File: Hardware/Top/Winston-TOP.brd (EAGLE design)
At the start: 38 x 38 mm, 52 parts, among them SW1 SWITCH.MOM, SW2 SWITCH.MOM, SW5 SWITCH.MOM, U2 NRF52832_MODULE_MDBT42, U4 PCF8523

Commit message: updated Hardware files
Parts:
- added C22: 100n, LinnesLab-Passives:C0603
- added C23, C24: 47p, LinnesLab-Passives:C0603
- added JP2: (no value), LinnesLab-Switches:SMT-JUMPER_2_NO_SILK
- added LED5: RED, LinnesLab-LED:LED-0603
- added LED6: YELLOW, LinnesLab-LED:LED-0603
- added R1, R2: 0, LinnesLab-Passives:R0603
- added R17, R18: 27, LinnesLab-Passives:R0603
- added R19, R20: 1k, LinnesLab-Passives:R0603
- added U5: FT231XS, LinnesLab-DigitalIC:SSOP20_L
- R8, R9: value 10k -> 10K
- moved R9 57.9 mm to (-16.1, -19.4), turned to 0 degrees
- moved R8 55.5 mm to (-16.1, -16.7), turned to 0 degrees
- moved L2 2.19 mm to (20.3, 25.8)
- moved U2 1.08 mm to (31.5, 29.2)
- moved C16 0.66 mm to (23.0, 26.0)
- moved C7 0.53 mm to (24.5, 26.0)
- moved R3 0.49 mm to (40.0, 24.9)
- moved C18 0.32 mm to (21.8, 25.6)
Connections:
- removed net RXD: U2.21
- removed net TXD: U2.19
- new net !CTS: JP2.2, U5.9
- new net FT3V3: U5.13
- new net N$23: R17.2, U5.12
- new net N$24: R18.2, U5.11
- new net N$25: LED5.C, R19.2
- new net N$26: LED6.C, R20.2
- new net RXD.FT: R2.1, U5.4
- new net RXD.NRF: R1.2, U2.21
- new net RXLED: R19.1, U5.17
- new net TXD.FT: R1.1, U5.20
- new net TXD.NRF: R2.2, U2.19
- new net TXLED: R20.1, U5.10
- net 3.3V: now also C22.2, LED5.A, LED6.A, U5.14, U5.3
- net DTR: now also U5.1
- net GND: now also C22.1, C23.2, C24.1, JP2.1, U5.16, U5.6
- net SCL: now also R9.1; no longer R8.1
- net SDA: now also R8.1; no longer R9.1
- net USB+: now also C23.1, R18.1
- net USB-: now also C24.2, R17.1
- net V_USB: now also U5.15

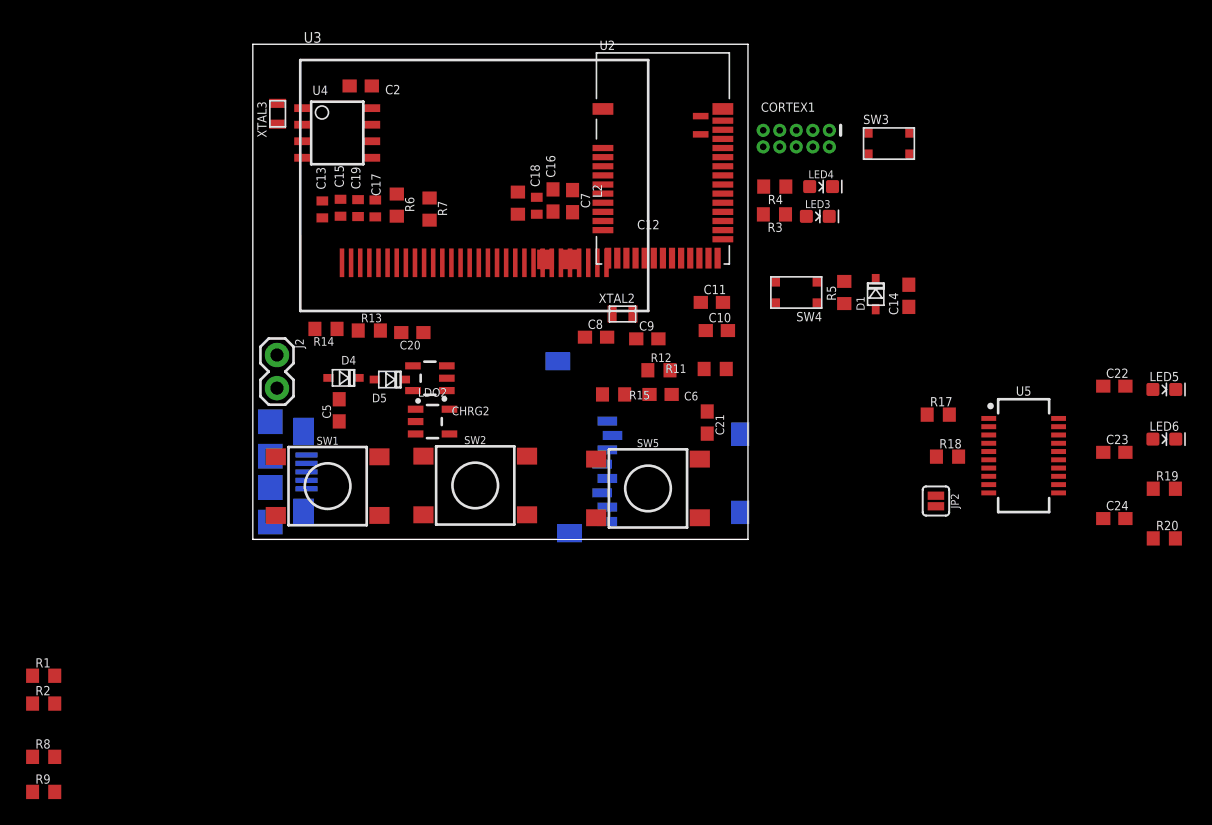
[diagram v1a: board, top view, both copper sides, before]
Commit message: updated top and bottom boards with everything from Take 002
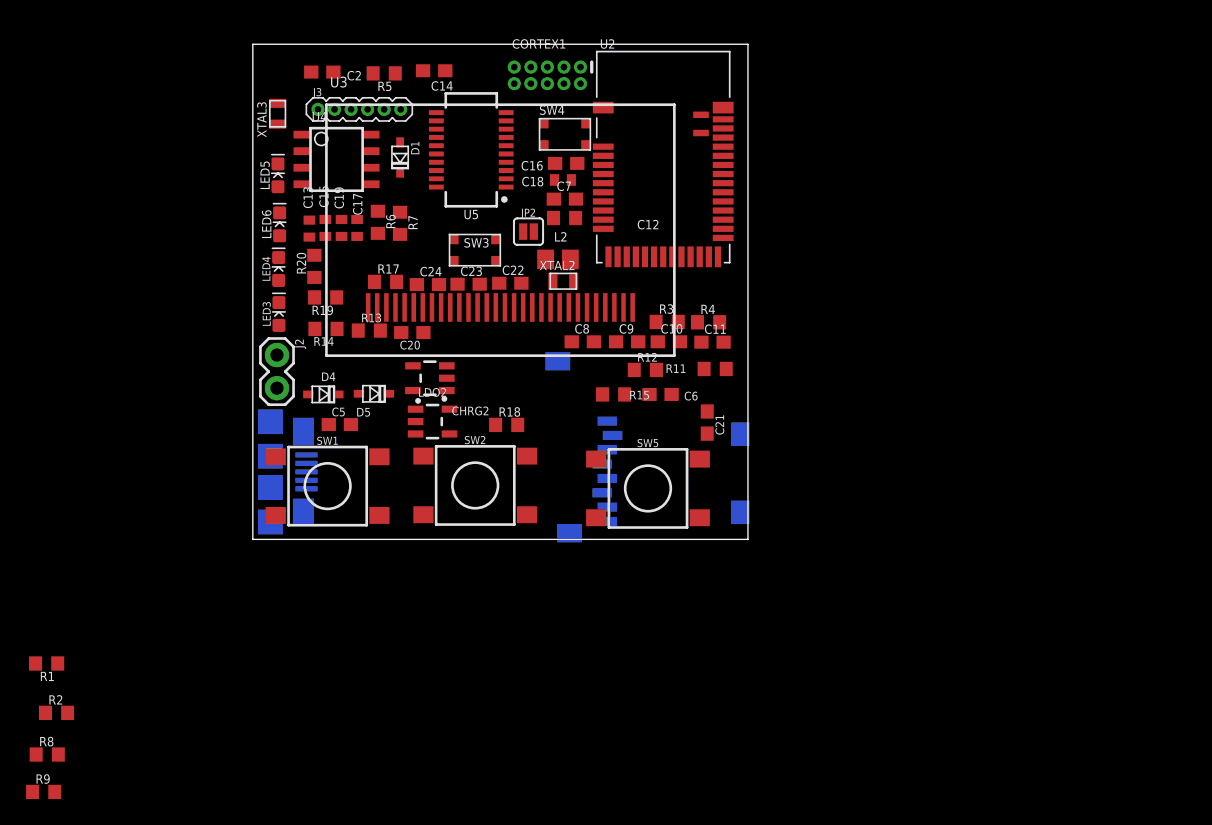
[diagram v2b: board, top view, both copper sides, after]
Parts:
- added J3: (no value), LinnesLab-Connectors:1X06_1.27MM
- moved LED5 70.0 mm to (1.93, 27.9), turned to 90 degrees
- moved LED6 69.9 mm to (2.06, 24.2), turned to 90 degrees
- moved R20 68.5 mm to (4.72, 21.0), turned to 90 degrees
- moved R19 66.0 mm to (5.59, 18.6), turned to 180 degrees
- moved C24 55.7 mm to (13.4, 19.6)
- moved C23 51.2 mm to (16.6, 19.6)
- moved U5 48.5 mm to (16.8, 29.9), turned to 90 degrees
- moved C22 47.0 mm to (19.8, 19.7)
- moved R17 43.6 mm to (10.2, 19.8)
- moved LED4 42.1 mm to (1.98, 20.8), turned to 90 degrees
- moved LED3 42.0 mm to (2.01, 17.3), turned to 90 degrees
- moved C14 40.3 mm to (13.9, 36.0), turned to 0 degrees
- moved R5 39.1 mm to (10.1, 35.8), turned to 180 degrees
- moved D1 38.0 mm to (11.3, 29.3), turned to 270 degrees
- moved JP2 37.5 mm to (21.2, 23.6), turned to 0 degrees
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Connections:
- removed net BATT: R13.1, R14.2
- removed net CD1: SD2.CD1
- removed net CHRG.STAT: CHRG2.1, R12.1
- removed net CS.OLED: U3.13
- removed net DC.OLED: U3.15
- removed net RESET.OLED: U3.14
- removed net SD.CS: SD2.2
- removed net SW1: SW1.A1, SW2.A1, SW5.A1
- new net A0/PPG: J3.5, U2.15
- new net A4/BATT: R13.1, R14.2, U2.5
- new net A7/TIA: J3.6, U2.8
- new net D11/SW1: SW1.A1, U2.25
- new net D15/SW2: SW2.A1, U2.29
- new net D16/SW3: SW5.A1, U2.30
- new net D27/CHRG.STATUS: CHRG2.1, R12.1, U2.4
- new net D29/LED.CTRL: J3.4, U2.6
- new net D3/RESET.OLED: U2.16, U3.14
- new net D30/CS.OLED: U2.7, U3.13
- new net D4/DC.OLED: U2.17, U3.15
- new net D5/CD1: SD2.CD1, U2.18
- new net D7/SD.CS: SD2.2, U2.20
- new net N$22: J3.3
- new net N$27: J3.2
- new net N$28: J3.1

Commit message: routed the top board
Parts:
- removed C13, C15, C17: 2.2uF, LinnesLab-Passives:C0402
- removed C14, C22: 100n, LinnesLab-Passives:C0603
- removed C16: 10uF, LinnesLab-Passives:C0603
- removed C23, C24: 47p, LinnesLab-Passives:C0603
- removed CHRG2: MCP73831, LinnesLab-Power:SOT23-5
- removed CORTEX1: CORTEX_DEBUG_PTH, LinnesLab-Connectors:2X5-PTH-1.27MM
- removed D4, D5: (no value), LinnesLab-DiscreteSemi:USC
- removed J3: (no value), LinnesLab-Connectors:1X06_1.27MM
- removed JP2: (no value), LinnesLab-Switches:SMT-JUMPER_2_NO_SILK
- removed L2: 10u, LinnesLab-Passives:L0603
- removed LDO2: MIC5504, LinnesLab-Power:SOT23-5
- removed LED5: RED, LinnesLab-LED:LED-0603
- removed LED6: YELLOW, LinnesLab-LED:LED-0603
- removed R19, R20: 1k, LinnesLab-Passives:R0603
- removed R5: 10k, LinnesLab-Passives:R0603
- removed R8, R9: 10K, LinnesLab-Passives:R0603
- removed U5: FT231XS, LinnesLab-DigitalIC:SSOP20_L
- removed USB2: USB.MICRO-BIGGERPADS, LinnesLab-Connectors:USB-MICRO-01.BIGGERPADS
- removed XTAL2: 32.768kHz, LinnesLab-Clocks:2-SMD.NOLEAD.2.0MMTO1.2MM
- removed XTAL3: 32.7680kHz, LinnesLab-Clocks:2-SMD.NOLEAD.2.0MMTO1.2MM
- added C1: 10uF, LinnesLab-Passives:C0603
- added C3, C4: 2.2uF, LinnesLab-Passives:C0402
- added D2, D3: (no value), LinnesLab-DiscreteSemi:USC
- added DEBUG1: CORTEX_DEBUG_PTH, LinnesLab-Connectors:2X5-PTH-1.27MM
- added J1: (no value), LinnesLab-Connectors:1X07_1.27MM
- added JP1: (no value), LinnesLab-Switches:SMT-JUMPER_2_NO_SILK
- added L1: 10u, LinnesLab-Passives:L0603
- added LED1: RED, LinnesLab-LED:LED-0603
- added LED2: BLUE, LinnesLab-LED:LED-0603
- added R10: 100k, LinnesLab-Passives:R0603
- added R16: 1k, LinnesLab-Passives:R0603
- added USB1: USB.MICRO-BIGGERPADS, LinnesLab-Connectors:USB-MICRO-01.BIGGERPADS
- added XTAL1: 32.768kHz, LinnesLab-Clocks:2-SMD.NOLEAD.2.0MMTO1.2MM
- C10: value 300p -> (none)
- C12: value 10u -> 300p; device LinnesLab-Passives:C0805 -> LinnesLab-Passives:C0603
- C18, C19: value 2.2uF -> 47p; device LinnesLab-Passives:C0402 -> LinnesLab-Passives:C0603
- C2, C5, C6: value 1u -> 2.2uF; device LinnesLab-Passives:C0603 -> LinnesLab-Passives:C0402
- C20, C21: value 4.7u -> 100n
- C8: value (none) -> 10u; device LinnesLab-Passives:C0603 -> LinnesLab-Passives:C0805
- LED4: value BLUE -> YELLOW
- R1: value 0 -> 10k
- R11: value (none) -> 100k
- R12, R13: value 100k -> 27
- R14: value 100k -> 10k
- R15: value 100k -> 1k
- R17, R18: value 27 -> 0
- R2: value 0 -> 390k
- R3, R4: value 1k -> 10K
- R6: value 10k -> 1k
- R7: value 390k -> 1k
- SW3: value (none) -> SWITCH.MOM; device LinnesLab-Switches:BUTTON-GULLWING -> LinnesLab-Switches:TACTILE_SWITCH_SMD_6.2MM_TALL
- SW5: value SWITCH.MOM -> (none); device LinnesLab-Switches:TACTILE_SWITCH_SMD_6.2MM_TALL -> LinnesLab-Switches:BUTTON-GULLWING
- U4: value PCF8523 -> FT231XS; device LinnesLab-Clocks:SO8 -> LinnesLab-DigitalIC:SSOP20_L
- moved R2 48.5 mm to (24.4, 14.8), turned to 270 degrees
- moved R1 44.6 mm to (15.8, 21.9), turned to 270 degrees
- moved R11 32.0 mm to (4.04, 19.0), turned to 90 degrees
- moved R14 30.0 mm to (35.0, 10.2), turned to 0 degrees
- moved R4 24.5 mm to (12.8, 27.1)
- moved C19 24.3 mm to (18.8, 2.79), turned to 0 degrees
- moved R7 24.3 mm to (35.5, 23.5), turned to 90 degrees
- moved R6 24.1 mm to (33.7, 23.5), turned to 90 degrees
- moved C18 23.0 mm to (18.8, 5.16)
- moved R3 22.8 mm to (12.7, 29.2)
- moved SW3 22.3 mm to (31.2, 5.01), turned to 180 degrees
- moved U4 22.0 mm to (10.0, 7.44), turned to 270 degrees
- moved D1 20.5 mm to (6.67, 9.31), flipped to the bottom
- moved C6 20.4 mm to (13.8, 21.5), turned to 270 degrees
- moved LED3 19.5 mm to (19.6, 8.94), turned to 180 degrees
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- renumbered SD2 to SD1, U3 to U1
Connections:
- removed net N$17: CHRG2.5, R11.2
- removed net N$19: U4.2, XTAL3.P$1
- removed net N$20: U4.1, XTAL3.P$2
- removed net N$22: J3.3
- removed net N$27: J3.2
- removed net N$28: J3.1
- removed net VBATT: U4.3
- net !CTS: now also JP1.2, U4.9; no longer JP2.2, U5.9
- net 3.3V: now also C20.2, C5.2, C6.2, C8.2, D3.-, DEBUG1.1, J1.4, LED3.A, LED4.A, R14.2, R3.2, R4.2, U4.14, U4.3; no longer C12.2, C17.2, C19.2, C2.1, C22.2, C6.1, CORTEX1.1, D1.-, LDO2.5, LED5.A, LED6.A, R15.2, R5.2, R8.2, R9.2, U4.8, U5.14, U5.3
- net A0/PPG: now also J1.7; no longer J3.5
- net A4/BATT: now also R10.1, R11.2; no longer R13.1, R14.2
- net A7/TIA: now also J1.6; no longer J3.6
- net D16/SW3: now also SW3.A1; no longer SW5.A1
- net D27/CHRG.STATUS: no longer CHRG2.1, R12.1
- net D29/LED.CTRL: now also J1.5; no longer J3.4
- net DFU: now also SW4.3; no longer SW3.3
- net DTR: now also C21.1, U4.1; no longer C14.1, U5.1
- net FT3V3: now also U4.13; no longer U5.13
- net GND: now also C1.1, C12.2, C19.2, C20.1, C3.1, C6.1, C9.1, DEBUG1.3, DEBUG1.5, DEBUG1.7, DEBUG1.9, J1.3, JP1.1, LED1.C, LED2.C, R1.1, R2.2, SW3.B1, SW3.B2, SW4.1, SW5.3, U4.16, U4.6, USB1.5; no longer C12.1, C16.1, C17.1, C19.1, C2.2, C20.2, C21.1, C22.1, C23.2, C24.1, C6.2, C9.2, CHRG2.2, CORTEX1.3, CORTEX1.5, CORTEX1.7, CORTEX1.9, JP2.1, LDO2.2, LED3.C, LED4.C, R14.1, R15.1, R6.1, R7.2, SW3.1, SW4.3, SW5.B1, SW5.B2, U4.4, U5.16, U5.6, USB2.5
- net LED1: now also R6.2; no longer R3.2
- net LED2: now also R7.2; no longer R4.2
- net N$1: now also R1.2; no longer R6.2
- net N$10: now also LED2.A, R7.1; no longer LED4.A, R4.1
- net N$11: now also L1.1; no longer L2.1
- net N$12: now also L1.2; no longer L2.2
- net N$13: now also C1.2; no longer C16.2
- net N$14: now also DEBUG1.8; no longer CORTEX1.8
- net N$15: now also C3.2; no longer C18.2
- net N$2: now also R2.1; no longer R7.1
- net N$23: now also R12.2, U4.12; no longer R17.2, U5.12
- net N$24: now also R13.2, U4.11; no longer R18.2, U5.11
- net N$25: now also LED3.C, R15.2; no longer LED5.C, R19.2
- net N$26: now also LED4.C, R16.2; no longer LED6.C, R20.2
- net N$3: now also C4.2; no longer C13.2
- net N$4: now also C9.2, XTAL1.P$1; no longer C8.2, XTAL2.P$1
- net N$5: now also C4.1; no longer C13.1
- net N$6: now also C10.1, XTAL1.P$2; no longer C9.1, XTAL2.P$2
- net N$7: now also C2.2; no longer C15.2
- net N$8: now also C2.1; no longer C15.1
- net N$9: now also LED1.A, R6.1; no longer LED3.A, R3.1
- net P0.10/NFC2: now also C12.1; no longer C10.1
- net RESET: now also C21.2, D3.+, DEBUG1.10, R14.1, SW5.1; no longer C14.2, CORTEX1.10, D1.+, R5.1, SW4.1
- net RXD.FT: now also R18.1, U4.4; no longer R2.1, U5.4
- net RXD.NRF: now also R17.2; no longer R1.2
- net RXLED: now also R15.1, U4.17; no longer R19.1, U5.17
- net SCL: now also J1.2, R4.1; no longer R9.1, U4.6
- net SDA: now also J1.1, R3.1; no longer R8.1, U4.5
- net SWCLK: now also DEBUG1.4; no longer CORTEX1.4
- net SWDIO: now also DEBUG1.2; no longer CORTEX1.2
- net SWO: now also DEBUG1.6; no longer CORTEX1.6
- net TXD.FT: now also R17.1, U4.20; no longer R1.1, U5.20
- net TXD.NRF: now also R18.2; no longer R2.2
- net TXLED: now also R16.1, U4.10; no longer R20.1, U5.10
- net USB+: now also C19.1, R13.1, USB1.3; no longer C23.1, R18.1, USB2.3
- net USB-: now also C18.2, R12.1, USB1.2; no longer C24.2, R17.1, USB2.2
- net VIN: now also D1.-, D2.-; no longer C21.2, C5.2, CHRG2.4, D4.-, D5.-, LDO2.1, LDO2.3, R12.2
- net VLIPO: now also D1.+, R10.2; no longer C20.1, CHRG2.3, D4.+, R13.2
- net V_USB: now also D2.+, U4.15, USB1.1; no longer D5.+, U5.15, USB2.1
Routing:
- net GND: track 0.00 -> 56.2 mm, vias 0 -> 30
- net SCK: track 0.00 -> 46.8 mm, vias 0 -> 3
- net MOSI: track 0.00 -> 44.3 mm, vias 0 -> 5
- net RESET: track 0.00 -> 31.4 mm, vias 0 -> 2
- net D11/SW1: track 0.00 -> 30.7 mm, vias 0 -> 2
- net D15/SW2: track 0.00 -> 30.3 mm, vias 0 -> 2
- net DTR: track 0.00 -> 29.8 mm, vias 0 -> 2
- net TXD.NRF: track 0.00 -> 29.4 mm, vias 0 -> 2
- net MISO: track 0.00 -> 29.0 mm, vias 0 -> 3
- net D5/CD1: track 0.00 -> 27.9 mm, vias 0 -> 1
- net RXD.NRF: track 0.00 -> 27.3 mm, vias 0 -> 2
- net D16/SW3: track 0.00 -> 26.8 mm, vias 0 -> 2
- net VLIPO: track 0.00 -> 24.2 mm, vias 0 -> 1
- net SCL: track 0.00 -> 23.8 mm, vias 0 -> 4
- net SDA: track 0.00 -> 23.3 mm, vias 0 -> 2
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- added copper zone on layer 1, net 3.3V
- added copper zone on layer 16, net GND

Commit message: finished routing all boards
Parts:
- removed C21: 100n, LinnesLab-Passives:C0603
- removed R18: 0, LinnesLab-Passives:R0603
- added C13, C16: 4.7u, LinnesLab-Passives:C0603
- added C14, C15: 1u, LinnesLab-Passives:C0603
- added C17: 47p, LinnesLab-Passives:C0603
- added CHRG1: MCP73831, LinnesLab-Power:SOT23-5
- added LDO1: MIC5504, LinnesLab-Power:SOT23-5
- added R5, R9: 100k, LinnesLab-Passives:R0603
- added R8: (no value), LinnesLab-Passives:R0603
- C19: value 47p -> 100n
- R11: value 100k -> 27
- R13: value 27 -> 10k
- R14: value 10k -> 1k
- R16: value 1k -> 0
- moved C20 29.8 mm to (35.2, 13.6), turned to 0 degrees
- moved R13 23.2 mm to (35.0, 10.2), turned to 0 degrees
- moved R14 18.7 mm to (16.4, 8.97)
- moved R11 17.7 mm to (15.1, 5.14), turned to 180 degrees
- moved C19 15.1 mm to (5.59, 10.2), turned to 270 degrees
- moved R15 11.1 mm to (6.96, 3.06), turned to 180 degrees
- moved R10 11.1 mm to (4.07, 18.1), turned to 90 degrees
- moved R16 10.5 mm to (10.9, 12.7), turned to 0 degrees
- moved R17 3.56 mm to (7.38, 12.9), turned to 180 degrees
- moved R12 3.21 mm to (13.1, 2.63), turned to 90 degrees
- moved C18 2.37 mm to (18.8, 2.79), turned to 0 degrees
- moved SD1 1.78 mm to (36.6, 1.35)
- moved C5 1.08 mm to (12.5, 20.5)
- moved C2 0.86 mm to (11.0, 20.9)
- moved J2 0.79 mm to (2.26, 14.9)
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- renumbered U4 to U3
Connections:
- new net N$16: CHRG1.5, R8.2
- net 3.3V: now also C15.1, C19.2, LDO1.5, R13.2; no longer C20.2, R14.2
- net A4/BATT: now also R10.2, R9.1; no longer R10.1, R11.2
- net D27/CHRG.STATUS: now also CHRG1.1, R5.1
- net DTR: now also C20.1; no longer C21.1
- net GND: now also C13.1, C14.1, C15.2, C16.2, C17.1, C18.2, C19.1, CHRG1.2, LDO1.2, R10.1, R8.1; no longer C18.1, C19.2, C20.1, R11.1
- net N$23: now also R11.2; no longer R12.2
- net N$24: now also R12.2; no longer R13.2
- net N$25: now also R14.2; no longer R15.2
- net N$26: now also R15.2; no longer R16.2
- net RESET: now also C20.2, R13.1; no longer C21.2, R14.1
- net RXD.FT: now also R17.1; no longer R18.1
- net RXD.NRF: now also R16.2; no longer R17.2
- net RXLED: now also R14.1; no longer R15.1
- net TXD.FT: now also R16.1; no longer R17.1
- net TXD.NRF: now also R17.2; no longer R18.2
- net TXLED: now also R15.1; no longer R16.1
- net USB+: now also C18.1, R12.1; no longer C19.1, R13.1
- net USB-: now also C17.2, R11.1; no longer C18.2, R12.1
- net VIN: now also C13.2, C14.2, CHRG1.4, LDO1.1, LDO1.3, R5.2
- net VLIPO: now also C16.1, CHRG1.3, R9.2; no longer R10.2
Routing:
- net VIN: track 0.00 -> 33.3 mm, vias 0 -> 4
- net D27/CHRG.STATUS: track 0.00 -> 21.6 mm, vias 0 -> 2
- net GND: track 56.2 -> 67.4 mm, vias 30 -> 34
- net VLIPO: track 24.2 -> 31.8 mm
- net MOSI: track 44.3 -> 41.3 mm
- net N$16: track 0.00 -> 2.82 mm
- net SCL: track 23.8 -> 22.0 mm
- net D5/CD1: track 27.9 -> 26.1 mm
- net RXD.NRF: track 27.3 -> 28.8 mm
- net SCK: track 46.8 -> 45.5 mm
- net SDA: track 23.3 -> 22.3 mm
- net A4/BATT: track 22.9 -> 23.8 mm
- net N$7: track 5.17 -> 6.00 mm
- net N$8: track 3.60 -> 2.77 mm
- net MISO: track 29.0 -> 29.7 mm
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
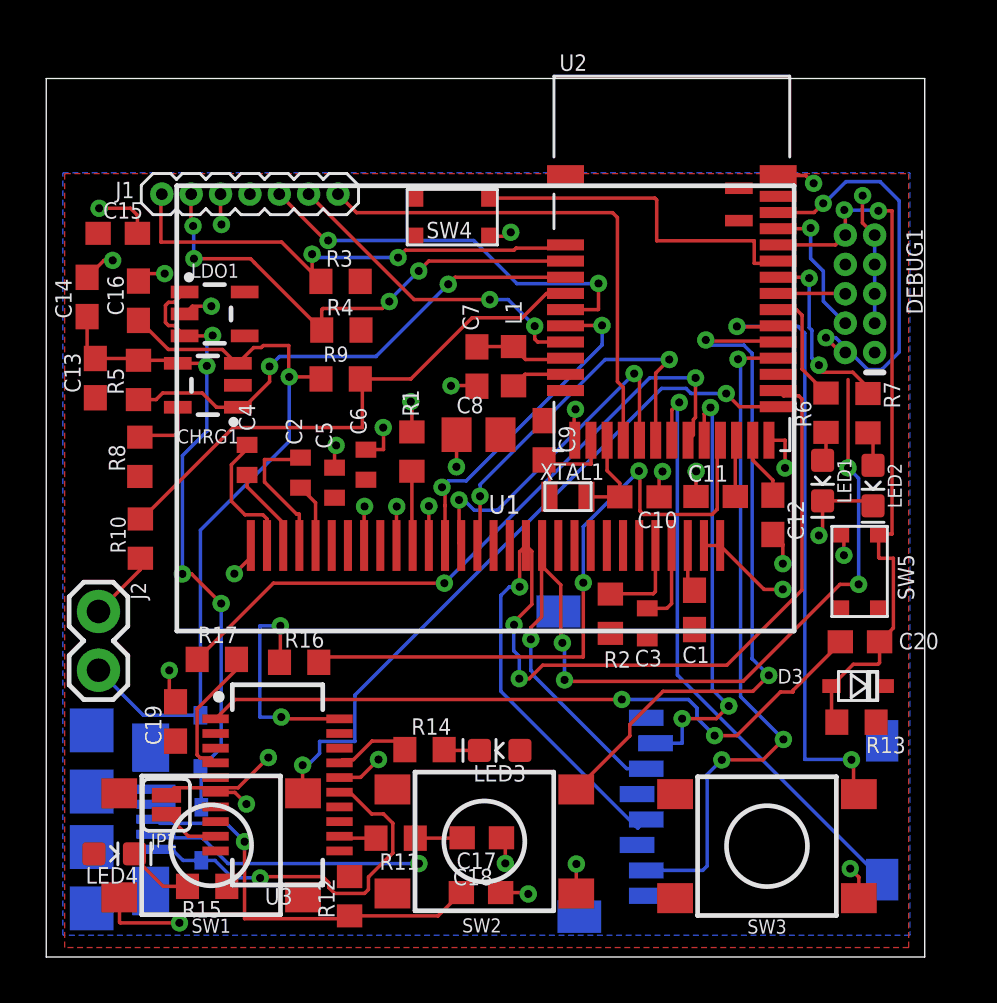
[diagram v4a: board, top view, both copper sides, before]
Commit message: continued routing top board
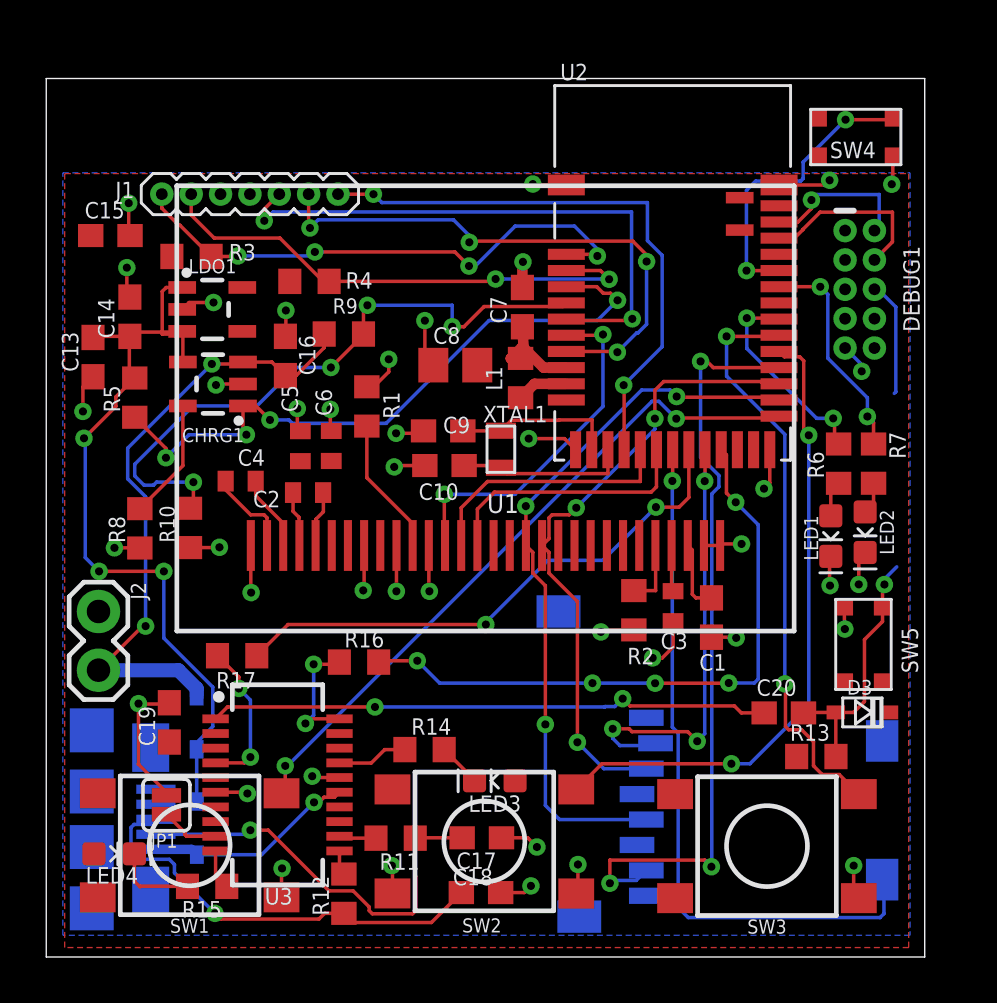
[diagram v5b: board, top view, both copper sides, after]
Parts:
- removed C11, C12: 300p, LinnesLab-Passives:C0603
- moved SW4 17.8 mm to (35.0, 35.5)
- moved C10 8.54 mm to (17.2, 21.3), turned to 180 degrees
- moved C16 6.79 mm to (10.3, 26.0)
- moved R3 6.54 mm to (6.28, 30.3), turned to 180 degrees
- moved C20 4.51 mm to (31.9, 10.6)
- moved C9 4.38 mm to (17.2, 22.8), turned to 0 degrees
- moved XTAL1 3.55 mm to (19.7, 22.0), turned to 270 degrees
- moved C7 3.24 mm to (20.6, 28.1), turned to 90 degrees
- moved C8 3.17 mm to (17.7, 25.6)
- moved SW5 3.16 mm to (35.3, 13.5)
- moved R8 3.09 mm to (4.05, 18.5)
- moved R1 2.76 mm to (13.9, 23.8)
- moved R16 2.59 mm to (13.5, 12.8)
- moved R4 2.52 mm to (11.4, 29.2), turned to 180 degrees
- moved LED1 2.43 mm to (33.9, 18.2)
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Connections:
- net GND: no longer C11.2, C12.2
- net P0.09/NFC1: no longer C11.1
- net P0.10/NFC2: no longer C12.1
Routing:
- net RESET: track 31.4 -> 11.2 mm, vias 2 -> 1
- net SCK: track 45.5 -> 31.1 mm
- net MOSI: track 41.3 -> 27.3 mm, vias 5 -> 3
- net SWDIO: track 17.8 -> 6.68 mm, vias 2 -> 1
- net A7/TIA: track 14.1 -> 24.1 mm, vias 2 -> 4
- net V_USB: track 16.4 -> 9.16 mm
- net D27/CHRG.STATUS: track 21.6 -> 28.7 mm, vias 2 -> 4
- net D29/LED.CTRL: track 18.0 -> 25.0 mm
- net TXD.NRF: track 29.4 -> 23.6 mm
- net DTR: track 30.0 -> 24.3 mm
- net D4/DC.OLED: track 16.8 -> 11.3 mm, vias 2 -> 0
- net VLIPO: track 31.8 -> 27.1 mm, vias 1 -> 2
- net TXD.FT: track 9.92 -> 5.42 mm
- net D5/CD1: track 26.1 -> 30.6 mm
- net A4/BATT: track 23.8 -> 28.0 mm, vias 0 -> 4
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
